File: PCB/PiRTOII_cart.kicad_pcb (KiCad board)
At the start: 2 copper layers, 58.2 x 77.5 mm, 6 parts, among them J1 2x22 card edge connector, J2 Conn_01x20, J3 Conn_01x20, Q1 BC547, SW1 SW_Push

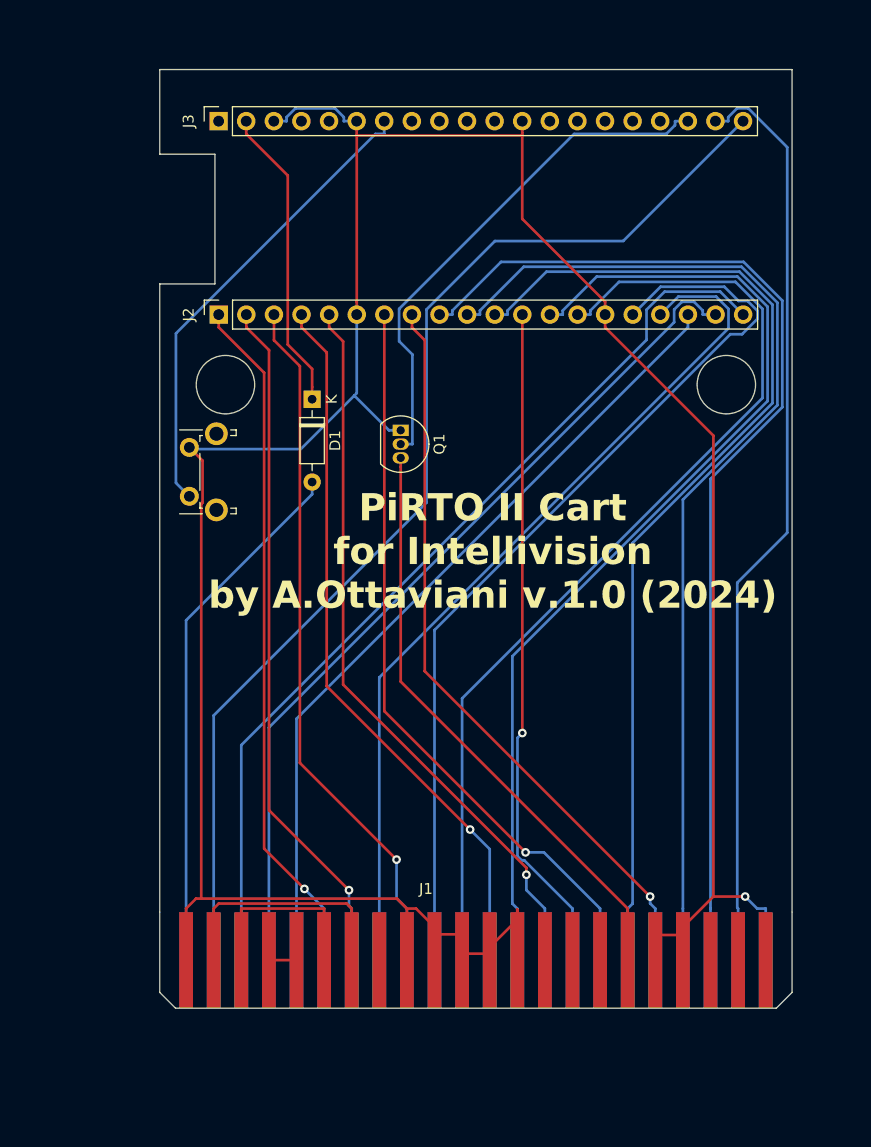
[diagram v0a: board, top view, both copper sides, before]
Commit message: Use original Pico board
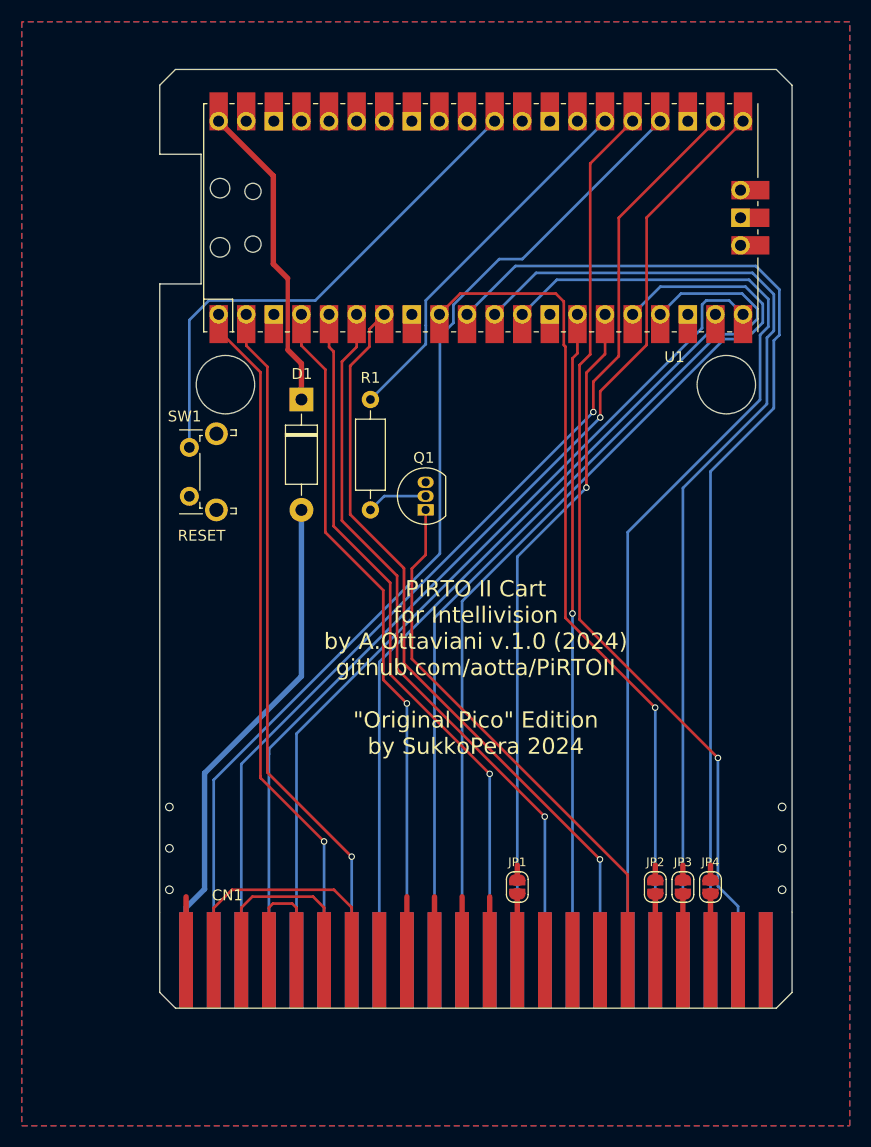
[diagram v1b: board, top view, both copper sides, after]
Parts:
- removed J2, J3: Conn_01x20, Connector_PinSocket_2.54mm:PinSocket_1x20_P2.54mm_Vertical
- added JP1: JMP_ROMDIS, Jumper:SolderJumper-2_P1.3mm_Open_RoundedPad1.0x1.5mm, F.Cu at (121.8, 181.2)
- added JP2: JMP_MCLK, Jumper:SolderJumper-2_P1.3mm_Open_RoundedPad1.0x1.5mm, F.Cu at (134.5, 181.2)
- added JP3: JMP_EXTVID, Jumper:SolderJumper-2_P1.3mm_Open_RoundedPad1.0x1.5mm, F.Cu at (137.0, 181.2)
- added JP4: JMP_EXTAUD, Jumper:SolderJumper-2_P1.3mm_Open_RoundedPad1.0x1.5mm, F.Cu at (139.6, 181.2)
- added R1: 100k, Resistor_THT:R_Axial_DIN0207_L6.3mm_D2.5mm_P10.16mm_Horizontal, F.Cu at (108.3, 136.4)
- added U1: PICO, MCU_RaspberryPi_and_Boards:RPi_Pico_SMD_TH, F.Cu at (118.5, 119.6)
- CN1: renamed from J1; value 2x22 card edge connector -> EDGE_CONN; footprint Evan's misc parts:edge mounted 44 pin card edge connector (2x22 pin) -> PiRTOII:Intellivision_Edge_Connector
- D1: value Diode -> 1n5819; footprint Diode_THT:D_DO-35_SOD27_P7.62mm_Horizontal -> Diode_THT:D_DO-41_SOD81_P10.16mm_Horizontal
- SW1: value SW_Push -> BTN_RESET_PICO
- moved Q1 7.68 mm to (113.4, 146.5), turned to 90 degrees
- moved D1 0.99 mm to (101.9, 136.4)
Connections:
- CN1 pad 10: GND -> Net-(CN1-MCLK)
- CN1 pad 12: rst' -> rst_inty'
- CN1 pad 20: GND -> Net-(CN1-ROM_DISABLE)
- CN1 pad 6: unconnected-(J1-Pin_6-Pad6) -> Net-(CN1-EXT_AUDIO)
- CN1 pad 8: GND -> Net-(CN1-EXT_VIDEO)
- Q1 pad 1: GND -> rst_inty'
- Q1 pad 2: Reset -> Net-(Q1-B)
- Q1 pad 3: rst' -> GND
- SW1 pad 1: RST -> GND
- SW1 pad 2: GND -> ~{RESET_PICO}
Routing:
- net GND: track 269.8 -> 34.6 mm, vias 1 -> 6
- net rst': track 54.9 -> 0.00 mm
- net rst_inty': track 0.00 -> 50.2 mm
- net Reset: track 48.0 -> 0.00 mm
- net ~{RESET_PICO}: track 0.00 -> 47.4 mm
- net RST: track 43.4 -> 0.00 mm
- net reset_inty_out: track 0.00 -> 34.6 mm
- net d11': track 92.9 -> 62.7 mm, vias 0 -> 1
- net bdir': track 80.1 -> 95.7 mm, vias 0 -> 1
- net Net-(CN1-BDIR_IN): track 2.54 -> 12.5 mm
- net bc2': track 85.8 -> 95.2 mm, vias 0 -> 1
- net bc1': track 104.3 -> 95.5 mm
- net d14': track 80.7 -> 72.2 mm
- net d6': track 68.7 -> 76.6 mm
- net Net-(CN1-ROM_DISABLE): track 0.00 -> 6.08 mm
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- added copper zone on B.Cu, net GND
- added copper zone on F.Cu, net GND
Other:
- outline, holes or cut-outs redrawn
- board text added: "PiRTO II Cart for Intellivision by A.Ottaviani v.1.0 (2024) github.com/aotta/PiRTOII {dblquote}Original Pico{dblquote} Edition by SukkoPera 2024"
- board text added: "RESET"
- board text removed: "PiRTO II Cart for Intellivision by A.Ottaviani v.1.0 (2024)"

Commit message: Almost there
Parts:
- added J1: CONN_SNOOP, Connector_PinHeader_2.54mm:PinHeader_2x22_P2.54mm_Vertical, F.Cu at (144.7, 173.2)
- added U2: 74LVC245, Package_DIP:DIP-20_W7.62mm_Socket_LongPads, F.Cu at (92.6, 166.8)
- added U3: 74LVC245, Package_DIP:DIP-20_W7.62mm_Socket_LongPads, F.Cu at (120.5, 166.8)
- added U4: 74LVC245, Package_DIP:DIP-20_W7.62mm_Socket_LongPads, F.Cu at (104.0, 154.1)
- moved R1 26.2 mm to (134.5, 136.4)
- moved Q1 22.5 mm to (134.5, 154.1)
- moved D1 8.02 mm to (99.4, 144.0)
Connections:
- net Net-(CN1-EXT_AUDIO) renamed /ext_audio
- net Net-(CN1-EXT_VIDEO) renamed /ext_video
- net Net-(CN1-MCLK) renamed /mclk
- net Net-(CN1-ROM_DISABLE) renamed /rom_disable
- CN1 pad 14: unconnected-(CN1-SR1_SEROUT-Pad14) -> /sr1
- CN1 pad 16: unconnected-(CN1-C3-Pad16) -> /c3
- CN1 pad 18: unconnected-(CN1-SERIN-Pad18) -> /serin
- CN1 pad 2: unconnected-(CN1-GND_EXTVIDEO_C1-Pad2) -> /c1
- CN1 pad 30: unconnected-(CN1-~{BUSAK_ROMCLK}-Pad30) -> /~{busak}
- CN1 pad 32: Net-(CN1-BC1_IN) -> bc1'
- CN1 pad 34: Net-(CN1-BC2_IN) -> bc2'
- CN1 pad 36: Net-(CN1-BDIR_IN) -> bdir'
- CN1 pad 38: Net-(CN1-BDIR_IN) -> bdir'
- CN1 pad 4: unconnected-(CN1-CBLNK_C2-Pad4) -> /c2
- CN1 pad 40: Net-(CN1-BC2_IN) -> bc2'
- CN1 pad 42: Net-(CN1-BC1_IN) -> bc1'
- U1 pad 1: d0' -> d0_lv
- U1 pad 10: d7' -> d7_lv
- U1 pad 11: d8' -> d8_lv
- U1 pad 12: d9' -> d9_lv
- U1 pad 14: d10' -> d10_lv
- U1 pad 15: d11' -> d11_lv
- U1 pad 16: d12' -> d12_lv
- U1 pad 17: d13' -> d13_lv
- U1 pad 19: d14' -> d14_lv
- U1 pad 2: d1' -> d1_lv
- U1 pad 20: d15' -> d15_lv
- U1 pad 21: bdir' -> bdir_lv
- U1 pad 22: bc2' -> bc2_lv
- U1 pad 24: bc1' -> bc1_lv
- U1 pad 25: ~{msync'} -> ~{msync_lv}
- U1 pad 34: unconnected-(U1-GPIO28_ADC2-Pad34)_0 -> DIR
- U1 pad 36: unconnected-(U1-3V3-Pad36) -> +3.3V
- U1 pad 4: d2' -> d2_lv
- U1 pad 5: d3' -> d3_lv
- U1 pad 6: d4' -> d4_lv
- U1 pad 7: d5' -> d5_lv
- U1 pad 9: d6' -> d6_lv
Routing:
- net DIR: track 0.00 -> 104.1 mm, vias 0 -> 2
- net +3.3V: track 0.00 -> 80.8 mm, vias 0 -> 1
- net bdir_lv: track 0.00 -> 69.1 mm
- net d9': track 90.9 -> 27.2 mm, vias 0 -> 1
- net bc2_lv: track 0.00 -> 63.5 mm
- net d8': track 92.8 -> 34.5 mm, vias 0 -> 1
- net bc1_lv: track 0.00 -> 54.6 mm
- net d7': track 95.8 -> 44.7 mm
- net ~{msync_lv}: track 0.00 -> 49.2 mm
- net d12': track 86.7 -> 42.2 mm, vias 0 -> 1
- net d10': track 59.7 -> 22.7 mm, vias 1 -> 0
- net d0_lv: track 0.00 -> 36.1 mm
- net d1': track 63.4 -> 27.3 mm, vias 1 -> 0
- net d15_lv: track 0.00 -> 35.8 mm
- net d13': track 83.8 -> 48.1 mm, vias 0 -> 1
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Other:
- board text added: "+5V"
- board text added: "BC1"
- board text added: "BC1_IN"
- board text added: "BC2"
- board text added: "BC2_IN"
- board text added: "BDIR"
- board text added: "BDIR_IN"
- board text added: "C3"
- board text added: "CBLNK/C2"
- board text added: "D0"
- board text added: "D1"
- board text added: "D10"
- board text added: "D11"
- board text added: "D12"
- board text added: "D13"
- board text added: "D14"
- board text added: "D15"
- board text added: "D2"
- board text added: "D3"
- board text added: "D4"
- board text added: "D5"
- board text added: "D6"
- board text added: "D7"
- board text added: "D8"
- board text added: "D9"
- board text added: "EXT_AUDIO"
- board text added: "EXT_VIDEO"
- board text added: "GND"
- board text added: "GND/EXT_VID/C1"
- board text added: "MCLK"
- board text added: "PiRTO II Cart for Intellivision by A. Ottaviani {dblquote}Original Pico{dblquote} Edition by SukkoPera 2024 github.com/SukkoPera/PiRTOII-OP"
- board text added: "ROM_DISABLE"
- board text added: "SER_IN"
- board text added: "SR1/SEROUT"
- board text added: "V1"
- board text added: "WARNING: Use original Pico board only!"
- board text added: "~{BUSAK}/ROMCLK"
- board text added: "~{MSYNC}"
- board text added: "~{RESET}"
- board text removed: "PiRTO II Cart for Intellivision by A.Ottaviani v.1.0 (2024) github.com/aotta/PiRTOII {dblquote}Original Pico{dblquote} Edition by SukkoPera 2024"

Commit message: Add MicroSD slot
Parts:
- added CN2: MICRO_SD_SLOT, PiRTOII:GCT-MEM2055-00-190-01-A, F.Cu at (131.4, 146.9)
- moved Q1 19.0 mm to (122.3, 139.5), turned to 0 degrees
- moved R1 3.13 mm to (132.5, 134.0), turned to 180 degrees
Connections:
- U1 pad 21: bdir_lv -> MISO
- U1 pad 22: bc2_lv -> CS
- U1 pad 24: bc1_lv -> SCK
- U1 pad 25: ~{msync_lv} -> MOSI
- U1 pad 27: unconnected-(U1-GPIO21-Pad27) -> ~{msync_lv}
- U1 pad 29: unconnected-(U1-GPIO22-Pad29) -> bdir_lv
- U1 pad 31: unconnected-(U1-GPIO26_ADC0-Pad31)_0 -> bc1_lv
- U1 pad 32: unconnected-(U1-GPIO27_ADC1-Pad32)_0 -> bc2_lv
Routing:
- net MISO: track 0.00 -> 48.3 mm, vias 0 -> 1
- net SCK: track 0.00 -> 44.9 mm, vias 0 -> 1
- net CS: track 0.00 -> 40.6 mm, vias 0 -> 1
- net MOSI: track 0.00 -> 38.6 mm, vias 0 -> 1
- net +3.3V: track 80.8 -> 110.5 mm, vias 1 -> 3
- net bc2_lv: track 63.5 -> 37.7 mm
- net bdir_lv: track 69.1 -> 49.8 mm
- net rst_inty': track 37.2 -> 56.2 mm, vias 0 -> 1
- net bc1_lv: track 54.6 -> 43.8 mm
- net ~{msync_lv}: track 49.2 -> 45.7 mm
- net reset_inty_out: track 27.5 -> 24.8 mm
- net d8_lv: track 33.1 -> 34.6 mm
- net Net-(Q1-B): track 7.31 -> 6.06 mm
- net d15_lv: track 35.8 -> 34.8 mm
- net d9_lv: track 34.7 -> 34.2 mm
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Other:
- board text added: "V2"
- board text removed: "V1"
